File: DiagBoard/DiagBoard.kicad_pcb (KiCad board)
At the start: 4 copper layers, 364 x 203 mm, 67 parts, among them J1 B1, P1 Conn_02x36_Top_Bottom, SW1 SW_DIP_x07, SW2 SW_Push_DPDT, SW3 SW_DIP_x04

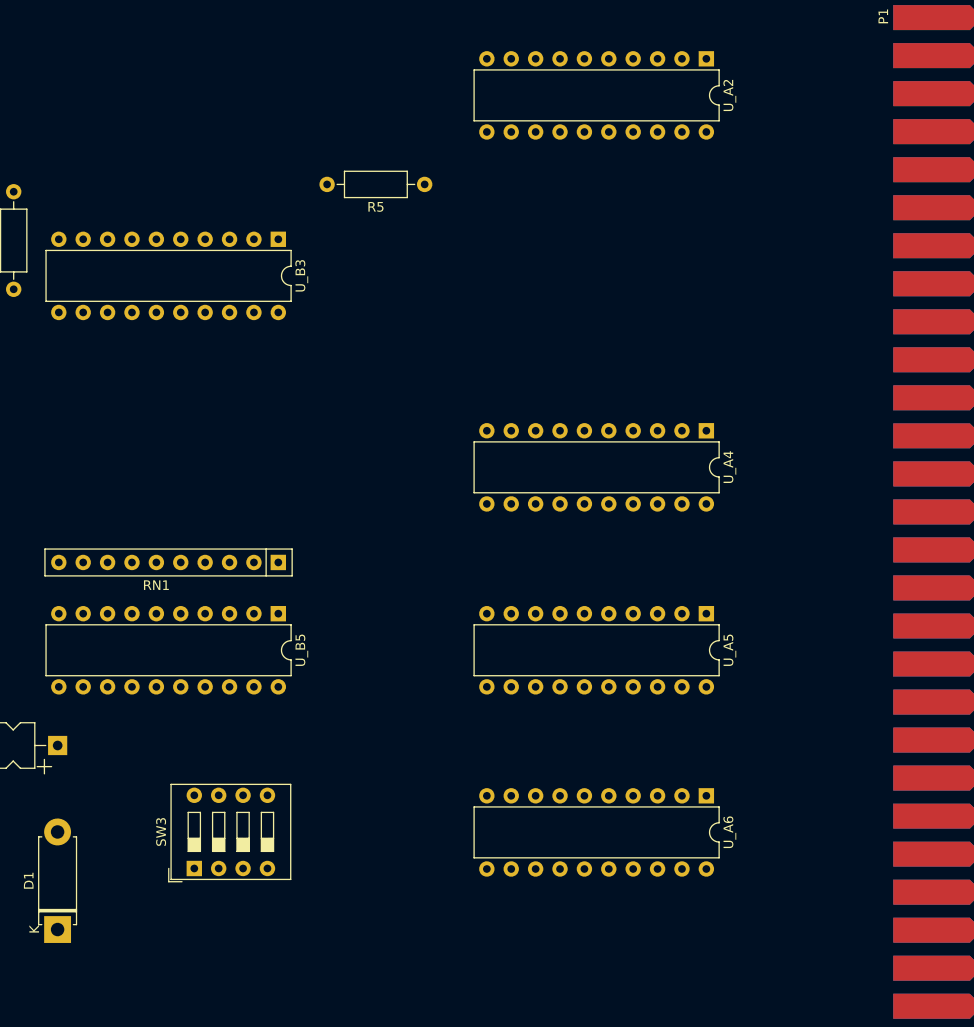
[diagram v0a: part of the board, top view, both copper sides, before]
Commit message: DiagBoard: Fix messed up address line
A11+A14, A12+A13
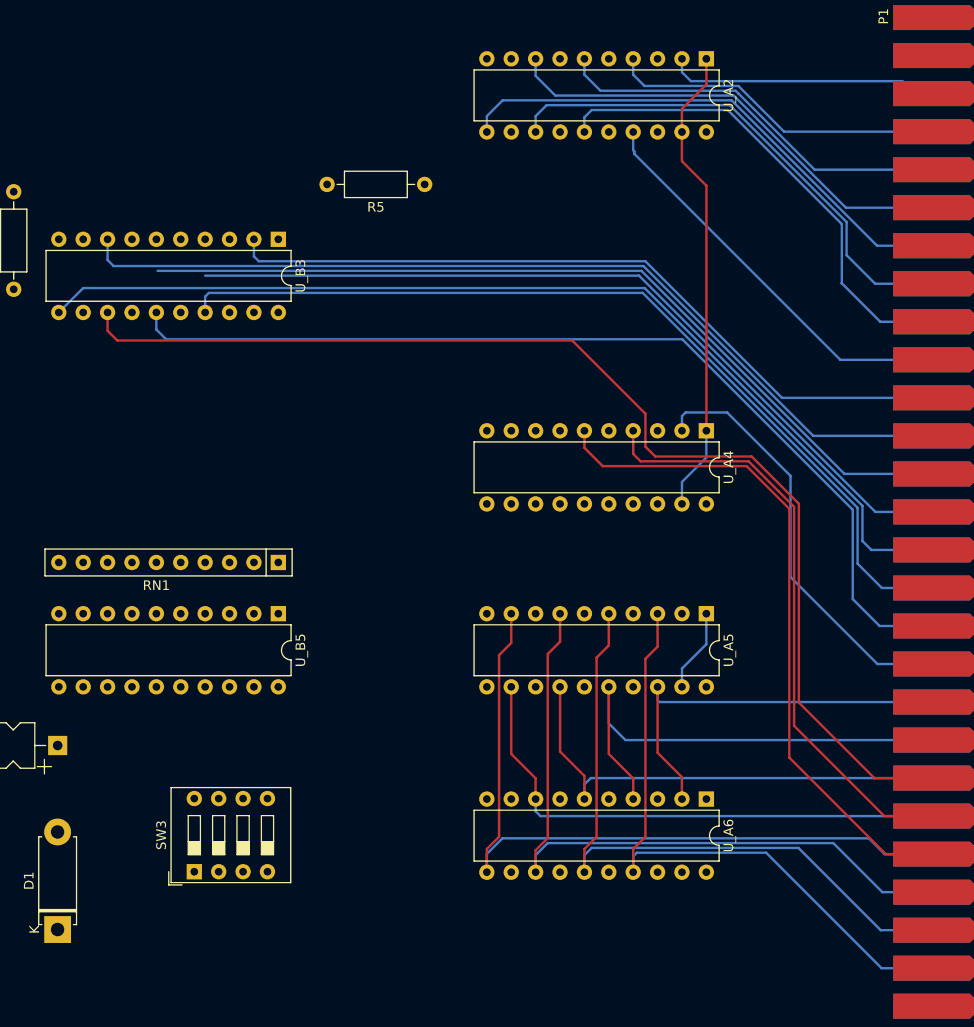
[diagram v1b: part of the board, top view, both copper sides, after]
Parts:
- moved SW3 0.34 mm to (306.2, 150.6)
- moved U_A6 0.34 mm to (359.5, 143.0)
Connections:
- U_B3 pad 3: /A12 -> /A13
- U_B3 pad 5: /A11 -> /A14
- U_E1 pad 10: /A12 -> /A13
- U_E1 pad 12: /A11 -> /A14
- U_E3 pad 3: /A12 -> /A13
- U_E3 pad 5: /A11 -> /A14
- U_E4 pad 3: /A12 -> /A13
- U_E4 pad 6: /A11 -> /A14
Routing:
- net /Sys.~{PA_{15}}: track 0.00 -> 119.4 mm
- net /Sys.~{A_{12}}: track 0.00 -> 103.6 mm
- net /Sys.~{A_{14}}: track 0.00 -> 99.0 mm
- net /Sys.~{A_{9}}: track 0.00 -> 93.8 mm
- net /Sys.~{A_{13}}: track 0.00 -> 91.9 mm
- net /Sys.~{A_{10}}: track 0.00 -> 87.6 mm
- net /Sys.~{A_{11}}: track 0.00 -> 84.1 mm
- net /Sys.~{A_{8}}: track 0.00 -> 76.7 mm
- net /Sys.~{D_{4}}: track 0.00 -> 75.8 mm
- net /Sys.~{D_{5}}: track 0.00 -> 71.9 mm
- net /Sys.~{PA_{17}}: track 0.00 -> 68.9 mm
- net /Sys.~{D_{6}}: track 0.00 -> 68.0 mm
- net /Sys.~{D_{7}}: track 0.00 -> 64.1 mm
- net /Sys.~{PA_{16}}: track 0.00 -> 60.7 mm
- net /Sys.~{D_{3}}: track 0.00 -> 53.7 mm
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
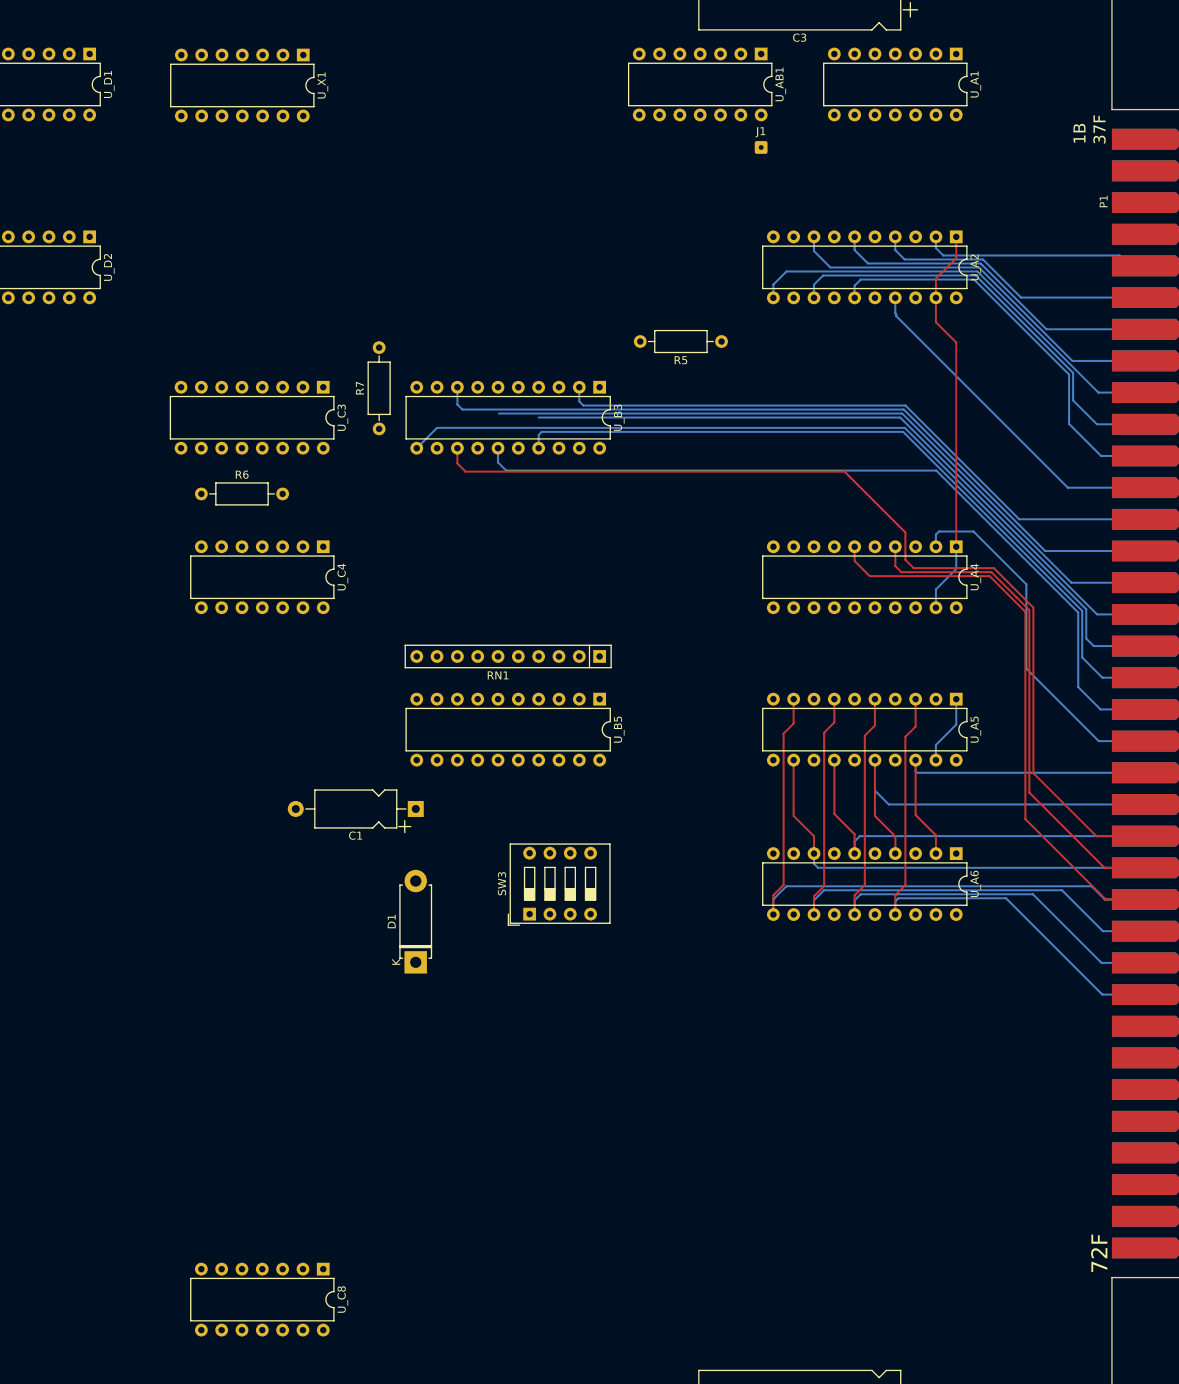
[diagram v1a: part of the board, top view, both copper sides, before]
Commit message: DiagBoard: Untwist U_B3 lines
Routes easier
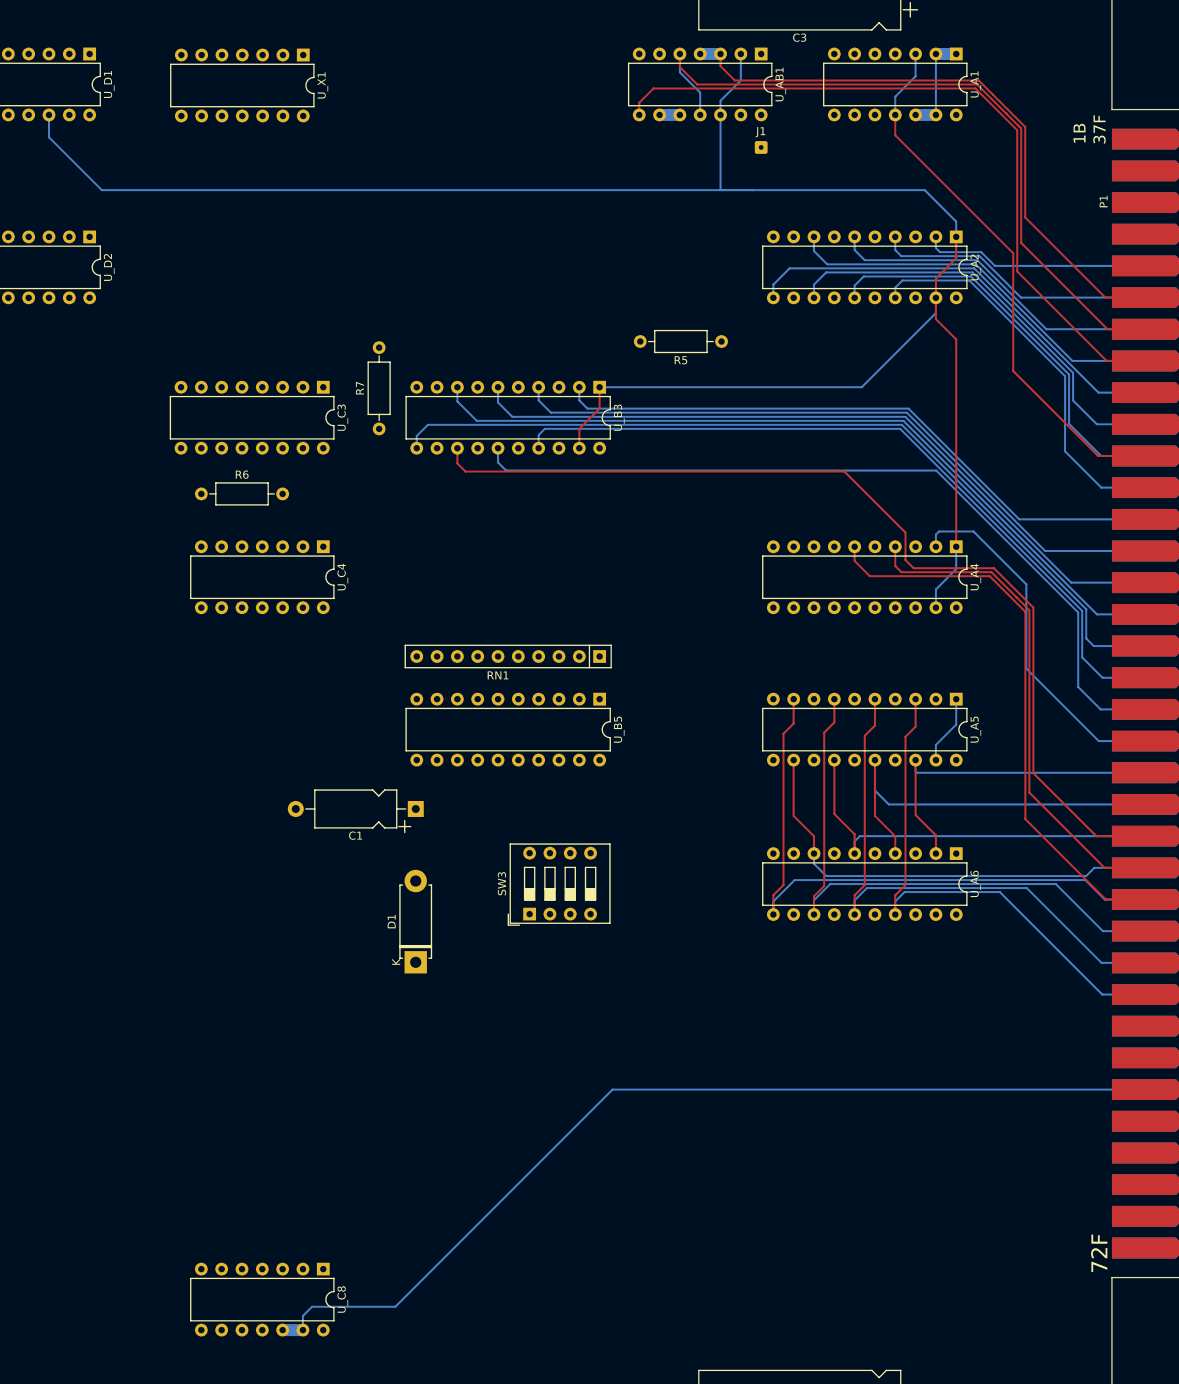
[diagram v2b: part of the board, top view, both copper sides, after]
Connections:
- U_B3 pad 12: /A9 -> /A11
- U_B3 pad 16: /A11 -> /A9
- U_B3 pad 4: /Sys.~{A_{11}} -> /Sys.~{A_{9}}
- U_B3 pad 8: /Sys.~{A_{9}} -> /Sys.~{A_{11}}
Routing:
- net /LOW: track 49.5 -> 250.6 mm
- net /Sys.5MHz: track 0.00 -> 119.4 mm
- net /Sys.~{WTIN}: track 0.00 -> 88.5 mm
- net /Sys.~{DRDY}: track 0.00 -> 88.0 mm
- net /Sys.~{RDIN}: track 0.00 -> 73.9 mm
- net /Sys.~{APRE}: track 0.00 -> 65.8 mm
- net /Sys.~{A_{11}}: track 84.1 -> 96.9 mm
- net /DIAG_MEM: track 0.00 -> 12.7 mm
- net /Sys.~{A_{9}}: track 93.8 -> 83.4 mm
- net /Sys.~{A_{7}}: track 40.4 -> 47.2 mm
- net /Sys.~{A_{10}}: track 87.6 -> 90.2 mm
- net /DRDY: track 0.00 -> 2.54 mm
- net /Sys.~{A_{12}}: track 103.6 -> 104.9 mm
- net /Sys.~{D_{3}}: track 53.7 -> 54.6 mm
- net /Sys.~{D_{7}}: track 64.1 -> 64.7 mm
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
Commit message: DiagBoard: Layout in progress
WIP dump. SRAM chips need replacement.
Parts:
- U_E1: footprint Package_DIP:DIP-16_W7.62mm -> Package_DIP:DIP-14_W7.62mm
- moved U_C8 94.9 mm to (251.2, 104.6)
- moved R2 70.2 mm to (27.1, 111.6)
- moved SW3 40.5 mm to (293.2, 112.3)
- moved R5 38.4 mm to (297.0, 98.3)
- moved R1 36.5 mm to (59.0, 103.5)
- moved RN2 34.9 mm to (40.1, 167.0), turned to -90 degrees
- moved R4 33.1 mm to (59.0, 97.9)
- moved D1 29.4 mm to (274.4, 133.0), turned to 0 degrees
- moved R3 28.7 mm to (43.2, 124.8)
- moved R7 24.3 mm to (310.2, 98.3), turned to 180 degrees
- moved R8 14.5 mm to (240.5, 58.2), turned to 180 degrees
- moved C1 14.0 mm to (284.4, 125.7)
- moved DIS1 7.83 mm to (30.5, 119.0)
- moved DIS2 7.82 mm to (30.5, 140.9)
- moved R6 1.20 mm to (266.3, 98.5)
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- renumbered U_X1 to U_C1
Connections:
- RN1 pad 3: /D0_O -> /D3_O
- RN1 pad 4: /D7_O -> /D2_O
- RN1 pad 5: /D6_O -> /D0_O
- RN1 pad 6: /D5_O -> /D7_O
- RN1 pad 8: /D2_O -> /D5_O
- RN1 pad 9: /D3_O -> /D6_O
- RN2 pad 10: Net-(RN2-R9) -> unconnected-(RN2-R9-Pad10)
- RN2 pad 2: unconnected-(RN2-R1-Pad2) -> Net-(D1-A)
- RN2 pad 3: Net-(D1-A) -> Net-(RN2-R2)
- SW1 pad 10: Net-(RN2-R7) -> Net-(RN2-R6)
- SW1 pad 11: Net-(RN2-R6) -> Net-(RN2-R5)
- SW1 pad 12: Net-(RN2-R5) -> Net-(RN2-R4)
- SW1 pad 13: Net-(RN2-R4) -> Net-(RN2-R3)
- SW1 pad 14: Net-(RN2-R3) -> Net-(RN2-R2)
- SW1 pad 8: Net-(RN2-R9) -> Net-(RN2-R8)
- SW1 pad 9: Net-(RN2-R8) -> Net-(RN2-R7)
- U_C1 pad 10: (no net) -> unconnected-(U_C1-Pad10)
- U_C1 pad 11: (no net) -> unconnected-(U_C1-Pad11)
- U_C1 pad 12: (no net) -> unconnected-(U_C1-Pad12)
- U_C1 pad 13: (no net) -> unconnected-(U_C1-Pad13)
- U_C1 pad 14: (no net) -> +5V
- U_C1 pad 4: (no net) -> unconnected-(U_C1-Pad4)
- U_C1 pad 5: (no net) -> unconnected-(U_C1-Pad5)
- U_C1 pad 6: (no net) -> unconnected-(U_C1-Pad6)
- U_C1 pad 7: (no net) -> GND
- U_C1 pad 8: (no net) -> unconnected-(U_C1-Pad8)
- U_C1 pad 9: (no net) -> unconnected-(U_C1-Pad9)
- U_E1 pad 14: (no net) -> +5V
- U_E1 pad 7: (no net) -> GND
- U_K7 pad 13: Net-(RN2-R6) -> Net-(RN2-R5)
- U_K7 pad 14: Net-(RN2-R7) -> Net-(RN2-R6)
- U_K7 pad 17: Net-(RN2-R8) -> Net-(RN2-R7)
- U_K7 pad 18: Net-(RN2-R9) -> Net-(RN2-R8)
- U_K7 pad 3: Net-(RN2-R5) -> Net-(RN2-R4)
- U_K7 pad 4: Net-(RN2-R4) -> Net-(RN2-R3)
- U_K7 pad 7: Net-(RN2-R3) -> Net-(RN2-R2)
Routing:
- net /A0: track 0.00 -> 539.8 mm
- net /A1: track 0.00 -> 519.6 mm
- net /A2: track 0.00 -> 519.5 mm
- net /A3: track 0.00 -> 517.1 mm
- net /A4: track 0.00 -> 508.7 mm
- net /A5: track 0.00 -> 507.9 mm
- net /A7: track 0.00 -> 503.1 mm
- net /A6: track 0.00 -> 478.0 mm
- net /A8: track 0.00 -> 459.6 mm
- net /D0_O: track 0.00 -> 456.9 mm, vias 0 -> 1
- net /A10: track 0.00 -> 449.8 mm, vias 0 -> 1
- net /A9: track 0.00 -> 446.2 mm, vias 0 -> 1
- net /D7_O: track 0.00 -> 435.4 mm, vias 0 -> 1
- net /D1_O: track 0.00 -> 426.6 mm
- net /D4_O: track 0.00 -> 415.4 mm
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
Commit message: DiagBoard: Signals layout complete
No power and ground yet. Fixed U_A2 type
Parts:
- U_F7, U_F8: footprint Package_DIP:DIP-18_W7.62mm -> ExtraFootprints:DIP-18_W10.16mm
- moved U_F8 1.27 mm to (185.2, 196.6)
- moved U_F7 0.65 mm to (185.2, 172.2)
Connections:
- U_F7 pad 11: /D5 -> /D4
- U_F7 pad 12: (no net) -> /D5
- U_F7 pad 9: /D4 -> GND
- U_F8 pad 11: /D2 -> /D3
- U_F8 pad 12: (no net) -> /D2
- U_F8 pad 9: /D3 -> GND
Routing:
- net GND: track 0.00 -> 178.9 mm
- net /RAM: track 144.0 -> 249.2 mm, vias 0 -> 2
- net /D3: track 387.0 -> 473.7 mm
- net /D2: track 370.4 -> 446.1 mm
- net /D1: track 368.0 -> 432.3 mm
- net /D0: track 357.2 -> 421.2 mm
- net /A2: track 519.5 -> 582.8 mm, vias 0 -> 1
- net /A4: track 508.7 -> 572.0 mm
- net /A6: track 478.0 -> 539.2 mm, vias 0 -> 1
- net +5V: track 0.00 -> 56.7 mm
- net /A5: track 507.9 -> 564.4 mm, vias 0 -> 1
- net Net-(U_F7-~{WE}): track 77.9 -> 131.7 mm, vias 0 -> 1
- net /A7: track 503.1 -> 556.0 mm, vias 0 -> 1
- net /A3: track 517.1 -> 568.1 mm
- net /A1: track 519.6 -> 570.6 mm
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- added copper zone on F.Cu, net +5V
- added copper zone on B.Cu, net GND
